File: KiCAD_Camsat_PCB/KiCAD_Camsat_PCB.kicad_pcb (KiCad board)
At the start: 2 copper layers, 92 parts, among them J1 Barrel_Jack, J3 105017-0001, J4 210-1S-1*3Ppin Gold-plated, J5 DZ127R-11-02-25, K1 HYC77-TF09-200, Q1 2N7002T-7-F, Q2 SS8050-G_C164885, Q3 BSS138, Q4 BSS138, Q8 2N7002T-7-F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

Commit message: New PCB design
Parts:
- removed ADDR0: JUMPER-SMT_3_1-NC_TRACE_SILK, Jumper:SolderJumper-2_P1.3mm_Bridged_Pad1.0x1.5mm
- removed C2, C26: 2u2, Capacitor_SMD:C_0603_1608Metric
- removed C21, C7: 100n, Capacitor_SMD:C_0603_1608Metric
- removed C3, C4: 10uF, Capacitor_SMD:C_0805_2012Metric
- removed D2: 1N4148, Diode_SMD:D_SOD-323
- removed D7: SS14, Diode_SMD:D_SMA
- removed J4: 210-1S-1*3Ppin Gold-plated, Connector_PinHeader_2.54mm:PinHeader_1x03_P2.54mm_Vertical
- removed JP1: SMD_JUMPER, Jumper:SolderJumper-2_P1.3mm_Open_Pad1.0x1.5mm
- removed JP9: SMD-JUMPER-CONNECTED_TRACE_SLODERMASK, Jumper:SolderJumper-2_P1.3mm_Bridged_Pad1.0x1.5mm
- removed Q3, Q4: BSS138, Package_TO_SOT_SMD:SOT-23
- removed R1, R5, R6: 10k, Resistor_SMD:R_0805_2012Metric
- removed R26, R27, R7, R8: 10K, Resistor_SMD:R_0805_2012Metric
- removed the R9 at (149.1, 68.8)
- removed the R9 at (189.1, 40.9)
- removed U2: MIC5225-3.3, Package_TO_SOT_SMD:SOT-23-5
- removed U3: SE5218, Package_TO_SOT_SMD:SOT-23-5
- removed U4: TXB0104QPWRQ1, esp32:SOP65P640X120-14N
- added R9: 10K, Resistor_SMD:R_0805_2012Metric, F.Cu at (76.2, 90.0)
- D3, D4, D9: value LESD5D5.0CT1G -> LESD
- J5: value DZ127R-11-02-25 -> DZ127R
- Q1, Q8: value 2N7002T-7-F -> 2N7002T
- Q2, Q9: value SS8050-G_C164885 -> SS8050
- U7: value AMS1117-3.3_C347222 -> AMS1117
- U9: value CP2102N-A02-GQFN28R -> CP2102N
- moved SW2 174.2 mm to (194.5, 72.2)
- moved SW1 168.5 mm to (195.0, 84.0)
- moved C20 158.9 mm to (202.0, 71.5), turned to 90 degrees
- moved D1 155.2 mm to (71.7, 24.0), turned to 0 degrees
- moved Q2 142.8 mm to (192.1, 62.6), turned to -90 degrees
- moved U8 139.8 mm to (164.8, 50.0)
- moved R18 128.5 mm to (191.5, 56.5), turned to 180 degrees
- moved C8 123.8 mm to (95.8, 133.5)
- moved C9 123.8 mm to (95.8, 136.0)
- moved C14 119.1 mm to (155.5, 77.3), turned to 90 degrees
- moved R25 118.7 mm to (106.9, 129.5)
- moved C15 118.7 mm to (146.5, 95.0), turned to 90 degrees
- moved C6 115.3 mm to (95.8, 131.0)
- moved C5 115.3 mm to (95.8, 128.5)
- moved D6 111.0 mm to (148.0, 74.0), turned to 180 degrees
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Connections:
- D1 pad 2: (no net) -> GND
- J1 pad 3: (no net) -> unconnected-(J1-Pad3)
- J3 pad P$1: (no net) -> GND
- J3 pad P$11: (no net) -> GND
- J3 pad P$12: (no net) -> GND
- J3 pad P$13: (no net) -> GND
- J3 pad P$2: (no net) -> GND
- K1 pad 9: (no net) -> unconnected-(K1-X-Pad9)
- K1 pad SHIELD: (no net) -> GND
- U1 pad 9: (no net) -> /INT2
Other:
- board outline added: 76 x 151.5 mm
- board text added: "2026 NAR CAMSAT"

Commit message: traces
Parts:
- moved C37 126.3 mm to (184.7, 70.0)
- moved D1 118.5 mm to (173.0, 85.5)
- moved R29 113.1 mm to (178.0, 44.5), turned to -90 degrees
- moved C8 111.5 mm to (146.5, 34.2), turned to -90 degrees
- moved R10 110.7 mm to (181.5, 59.0)
- moved R16 109.7 mm to (184.1, 56.5)
- moved C6 108.8 mm to (177.7, 59.5)
- moved R3 105.4 mm to (180.6, 70.0)
- moved C9 104.1 mm to (186.0, 84.0), turned to 90 degrees
- moved R20 103.8 mm to (176.5, 38.0), turned to 90 degrees
- moved R9 102.3 mm to (176.5, 70.0)
- moved R15 100.3 mm to (163.5, 33.5)
- moved LED1 99.2 mm to (168.9, 33.5)
- moved R4 95.9 mm to (172.0, 91.0)
- moved C16 93.7 mm to (154.0, 47.5), turned to -90 degrees
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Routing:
- net GND: track 0.00 -> 499.2 mm, vias 0 -> 5
- net +3V3: track 0.00 -> 259.4 mm, vias 0 -> 5
- net /EN: track 0.00 -> 90.1 mm, vias 0 -> 2
- net 3.3V: track 0.00 -> 71.6 mm
- net /IO4: track 0.00 -> 68.9 mm, vias 0 -> 1
- net /RTS: track 0.00 -> 68.8 mm, vias 0 -> 2
- net Net-(Q1-G): track 0.00 -> 68.7 mm, vias 0 -> 2
- net /DTR: track 0.00 -> 67.4 mm, vias 0 -> 2
- net /IO13: track 0.00 -> 65.6 mm, vias 0 -> 2
- net /IO22: track 0.00 -> 50.3 mm, vias 0 -> 5
- net /IO21: track 0.00 -> 49.9 mm, vias 0 -> 3
- net /TXD0: track 0.00 -> 48.7 mm, vias 0 -> 4
- net +5V_VBUS: track 0.00 -> 47.0 mm, vias 0 -> 2
- net /IO0_BTN: track 0.00 -> 46.2 mm, vias 0 -> 2
- net /USB_DP: track 0.00 -> 43.7 mm, vias 0 -> 2
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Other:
- board size 76 x 151.5 mm -> 76 x 78 mm

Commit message: PCB changes
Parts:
- moved R13 66.2 mm to (192.0, 90.0), turned to 90 degrees
- moved J3 2.03 mm to (139.0, 31.0)
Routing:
- net /IO13: track 65.6 -> 51.4 mm
- net /IO0: track 33.5 -> 19.8 mm
- net /EN: track 90.1 -> 103.7 mm, vias 2 -> 3
- net /USB_DP: track 43.7 -> 31.1 mm, vias 2 -> 0
- net /IO4: track 68.9 -> 57.4 mm
- net /RTS: track 68.8 -> 60.9 mm
- net /TXD: track 38.4 -> 45.6 mm, vias 2 -> 6
- net /IO0_BTN: track 46.2 -> 51.8 mm
- net /IO22: track 50.3 -> 55.3 mm, vias 5 -> 4
- net GND: track 499.2 -> 494.5 mm, vias 5 -> 40
- net /TXD0: track 48.7 -> 44.2 mm, vias 4 -> 2
- net /DTR: track 67.4 -> 71.7 mm
- net Net-(Q1-G): track 68.7 -> 64.9 mm, vias 2 -> 1
- net +5V_VBUS: track 47.0 -> 50.6 mm
- net /RXD: track 13.5 -> 17.0 mm, vias 2 -> 0
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- added copper zone on B.Cu, net GND
- added copper zone on F.Cu, net GND
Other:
- board size 76 x 78 mm -> 76 x 80.5 mm
- board text added: "Reset"

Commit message: Prototype
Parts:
- moved R19 5.02 mm to (156.6, 33.8)
- moved D9 3.54 mm to (132.0, 52.5), turned to 0 degrees
- moved D4 3.20 mm to (132.0, 48.8)
- moved C25 0.50 mm to (129.5, 39.5)
- moved J3 0.50 mm to (139.0, 31.5)
- turned D3 to 0 degrees
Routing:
- net /TXD: track 45.6 -> 34.9 mm, vias 6 -> 2
- net /EN: track 103.7 -> 93.6 mm
- net GND: track 494.5 -> 488.7 mm, vias 40 -> 34
- net /IO0_BTN: track 51.8 -> 46.5 mm
- net /USB_DP: track 31.1 -> 26.5 mm
- net /USB_DN: track 31.3 -> 27.6 mm
- net /RXD: track 17.0 -> 19.3 mm
- net +3V3: track 262.6 -> 262.1 mm
- net /TXD0: vias 2 -> 0

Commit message: new changes
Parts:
- removed R19, R20: 0Ω, Resistor_SMD:R_0805_2012Metric
- D3, D4, D9: value LESD -> LESD5D5.0CT1G
- J5: value DZ127R -> DZ127R-11-02-25
- Q1, Q8: value 2N7002T -> 2N7002T-7-F
- Q2, Q9: value SS8050 -> SS8050-G_C164885
- U7: value AMS1117 -> AMS1117-3.3_C347222
- U9: value CP2102N -> CP2102N-A02-GQFN28R
- moved D4 14.7 mm to (140.8, 37.0)
- moved D9 11.9 mm to (138.0, 42.2)
- moved Q1 10.2 mm to (138.6, 37.0), turned to 90 degrees
- moved R21 5.53 mm to (133.5, 45.4)
- moved C17 1.00 mm to (150.0, 48.0)
- moved C16 0.81 mm to (153.2, 47.4)
- moved R11 0.72 mm to (136.6, 48.6)
- moved C25 0.32 mm to (129.6, 39.2), turned to -90 degrees
- moved R22 0.20 mm to (147.2, 48.9)
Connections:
- C37 pad 1: 3.3V -> +3V3
- C5 pad 1: 3.3V -> +3V3
- C6 pad 1: 3.3V -> +3V3
- R2 pad 2: 3.3V -> +3V3
- R25 pad 2: 3.3V -> +3V3
- R3 pad 2: 3.3V -> +3V3
- R39 pad 2: 3.3V -> +3V3
- R4 pad 2: 3.3V -> +3V3
- R9 pad 2: 3.3V -> +3V3
- U1 pad 5: 3.3V -> +3V3
- U1 pad 8: 3.3V -> +3V3
- U10 pad 6: 3.3V -> +3V3
- U10 pad 8: 3.3V -> +3V3
- U8 pad 35: /TXD0 -> /RXD
- U9 pad 26: /TXD -> /RXD0
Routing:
- net GND: track 488.7 -> 0.00 mm, vias 34 -> 0
- net 3.3V: track 69.4 -> 0.00 mm
- net /TXD0: track 44.2 -> 0.00 mm
- net /RXD0: track 16.1 -> 54.0 mm, vias 0 -> 4
- net +3V3: track 262.1 -> 297.0 mm
- net /TXD: track 34.9 -> 0.00 mm, vias 2 -> 0
- net /RXD: track 19.3 -> 43.7 mm, vias 0 -> 2
- net /IO22: track 55.3 -> 41.8 mm, vias 4 -> 3
- net /USB_DP: track 26.5 -> 13.8 mm
- net /USB_DN: track 27.6 -> 37.2 mm, vias 3 -> 2
- net +5V_VBUS: track 50.3 -> 41.8 mm
- net /EN: track 93.6 -> 99.8 mm, vias 3 -> 2
- net /IO5: track 43.2 -> 37.8 mm
- net /IO21: track 48.7 -> 43.7 mm, vias 3 -> 2
- net Net-(Q1-G): track 64.7 -> 69.3 mm
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
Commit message: DRC update
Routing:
- net GND: track 0.00 -> 47.3 mm, vias 0 -> 7
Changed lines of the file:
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@@
 		(tags "SOT-523")
 		(property "Reference" "Q1"
-			(at -2.145 1 0)
+			(at 0.4 -1.6 0)
 			(layer "F.SilkS")
 			(effects
@@
 		(tags "Diode SOD523")
 		(property "Reference" "D4"
-			(at -2.2 0 180)
+			(at 0.4 1.8 180)
 			(layer "F.SilkS")
 			(effects
@@
 	)
 	(segment
+		(start 180.9 44.9)
+		(end 180.9 44.6)
+		(width 0.2)
+		(layer "F.Cu")
+		(net 1)
+	)
+	(segment
+		(start 146.5 33.45)
+		(end 147.75 33.45)
+		(width 0.2)
+		(layer "F.Cu")
+		(net 1)
+	)
+	(segment
+		(start 134.425 48.0375)
+		(end 134.425 45.4)
+		(width 0.2)
+		(layer "F.Cu")
+		(net 1)
+	)
+	(segment
+		(start 136 43.8)
+		(end 137.3 42.5)
+		(width 0.2)
+		(layer "F.Cu")
+		(net 1)
+	)
+	(segment
+		(start 136 43.8)
+		(end 134.425 45.375)
+		(width 0.2)
+		(layer "F.Cu")
+		(net 1)
+	)
+	(segment
+		(start 174.25 46.99)
+		(end 175.44 45.8)
+		(width 0.2)
+		(layer "F.Cu")
+		(net 1)
+	)
+	(segment
+		(start 179.4 46.4)
+		(end 180.9 44.9)
+		(width 0.2)
+		(layer "F.Cu")
+		(net 1)
+	)
+	(segment
+		(start 135.9 49.5125)
+		(end 134.425 48.0375)
+		(width 0.2)
+		(layer "F.Cu")
+		(net 1)
+	)
+	(segment
+		(start 147.75 33.45)
+		(end 149.4 31.8)
+		(width 0.2)
+		(layer "F.Cu")
+		(net 1)
+	)
+	(segment
+		(start 136.6 49.5125)
+		(end 135.9 49.5125)
+		(width 0.2)
+		(layer "F.Cu")
+		(net 1)
+	)
+	(segment
+		(start 134.425 45.375)
+		(end 134.425 45.4)
+		(width 0.2)
+		(layer "F.Cu")
+		(net 1)
+	)
+	(segment
+		(start 175.44 45.8)
+		(end 176 45.8)
+		(width 0.2)
+		(layer "F.Cu")
+		(net 1)
+	)
+	(segment
+		(start 137.3 42.5)
+		(end 137.3 42.2)
+		(width 0.2)
+		(layer "F.Cu")
+		(net 1)
+	)
+	(via
+		(at 131.2 45.6)
+		(size 0.6)
+		(drill 0.3)
+		(layers "F.Cu" "B.Cu")
+		(free yes)
+		(net 1)
+	)
+	(via
+		(at 140.2 39.2)
+		(size 0.6)
+		(drill 0.3)
+		(layers "F.Cu" "B.Cu")
+		(free yes)
+		(net 1)
+	)
+	(via
+		(at 179.4 46.4)
+		(size 0.6)
+		(drill 0.3)
+		(layers "F.Cu" "B.Cu")
+		(net 1)
+	)
+	(via
+		(at 149.4 31.8)
+		(size 0.6)
+		(drill 0.3)
+		(layers "F.Cu" "B.Cu")
+		(free yes)
+		(net 1)
+	)
+	(via
+		(at 136 43.8)
+		(size 0.6)
+		(drill 0.3)
+		(layers "F.Cu" "B.Cu")
+		(free yes)
+		(net 1)
+	)
+	(via
+		(at 176 45.8)
+		(size 0.6)
+		(drill 0.3)
+		(layers "F.Cu" "B.Cu")
+		(net 1)
+	)
+	(via
+		(at 131.2 39.8)
+		(size 0.6)
+		(drill 0.3)
+		(layers "F.Cu" "B.Cu")
+		(free yes)
+		(net 1)
+	)
+	(segment
+		(start 131.2 39.8)
+		(end 131.2 39.5)
+		(width 0.2)
+		(layer "B.Cu")
+		(net 1)
+	)
+	(segment
+		(start 141.5 34.2)
+		(end 142.4 35.1)
+		(width 0.2)
+		(layer "B.Cu")
+		(net 1)
+	)
+	(segment
+		(start 176 45.8)
+		(end 178.8 45.8)
+		(width 0.2)
+		(layer "B.Cu")
+		(net 1)
+	)
+	(segment
+		(start 134.2 45.6)
+		(end 136 43.8)
+		(width 0.2)
+		(layer "B.Cu")
+		(net 1)
+	)
+	(segment
+		(start 142.4 35.1)
+		(end 142.4 37.2)
+		(width 0.2)
+		(layer "B.Cu")
+		(net 1)
+	)
+	(segment
+		(start 140.4 39.2)
+		(end 140.2 39.2)
+		(width 0.2)
+		(layer "B.Cu")
+		(net 1)
+	)
+	(segment
+		(start 131.2 45.6)
+		(end 134.2 45.6)
+		(width 0.2)
+		(layer "B.Cu")
+		(net 1)
+	)
+	(segment
+		(start 131.2 39.8)
+		(end 131.2 45.6)
+		(width 0.2)
+		(layer "B.Cu")
+		(net 1)
+	)
+	(segment
+		(start 131.2 39.5)
+		(end 136.5 34.2)
+		(width 0.2)
+		(layer "B.Cu")
+		(net 1)
+	)
+	(segment
+		(start 178.8 45.8)
+		(end 179.4 46.4)
+		(width 0.2)
+		(layer "B.Cu")
+		(net 1)
+	)
+	(segment
+		(start 142.4 37.2)
+		(end 140.4 39.2)
+		(width 0.2)
+		(layer "B.Cu")
+		(net 1)
+	)
+	(segment

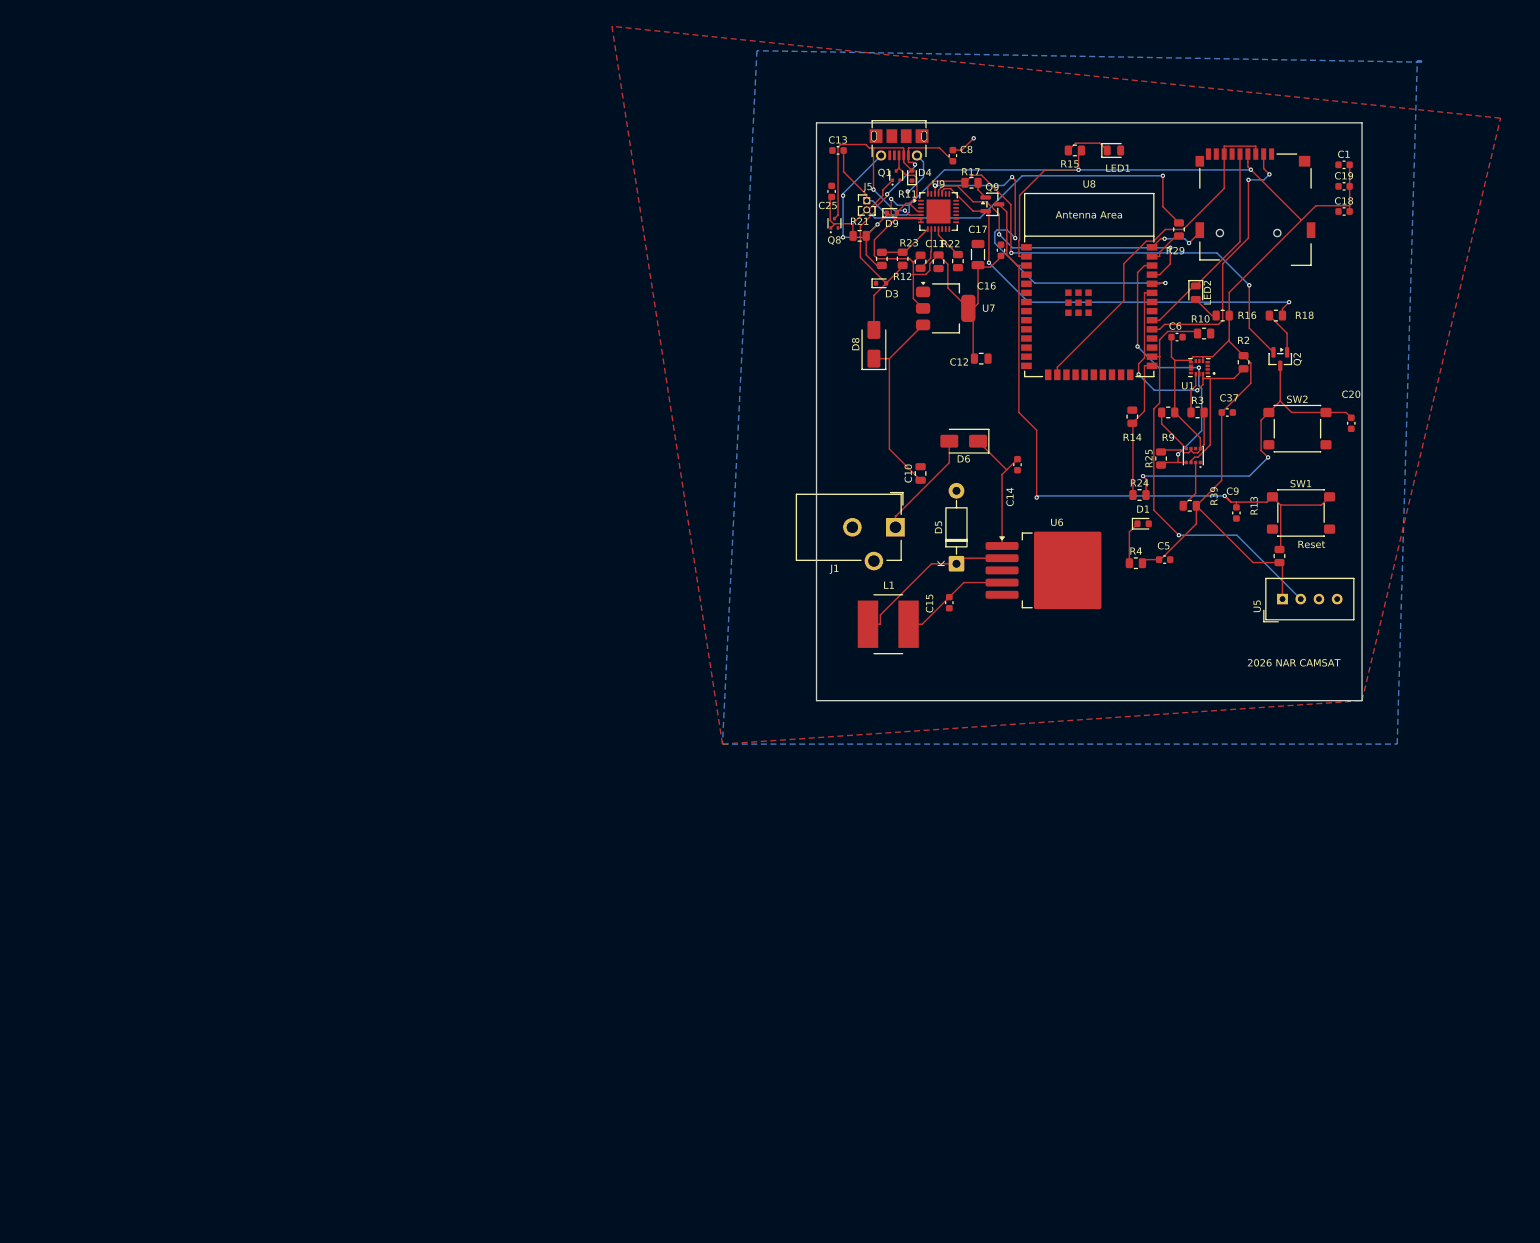
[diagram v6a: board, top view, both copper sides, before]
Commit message: Layout Revision
Removed unnecessary nets.
Added nets for copper pours.
Removed some non-critical components from schematic.
Still needs some extra vias and adjusting silkscreen.
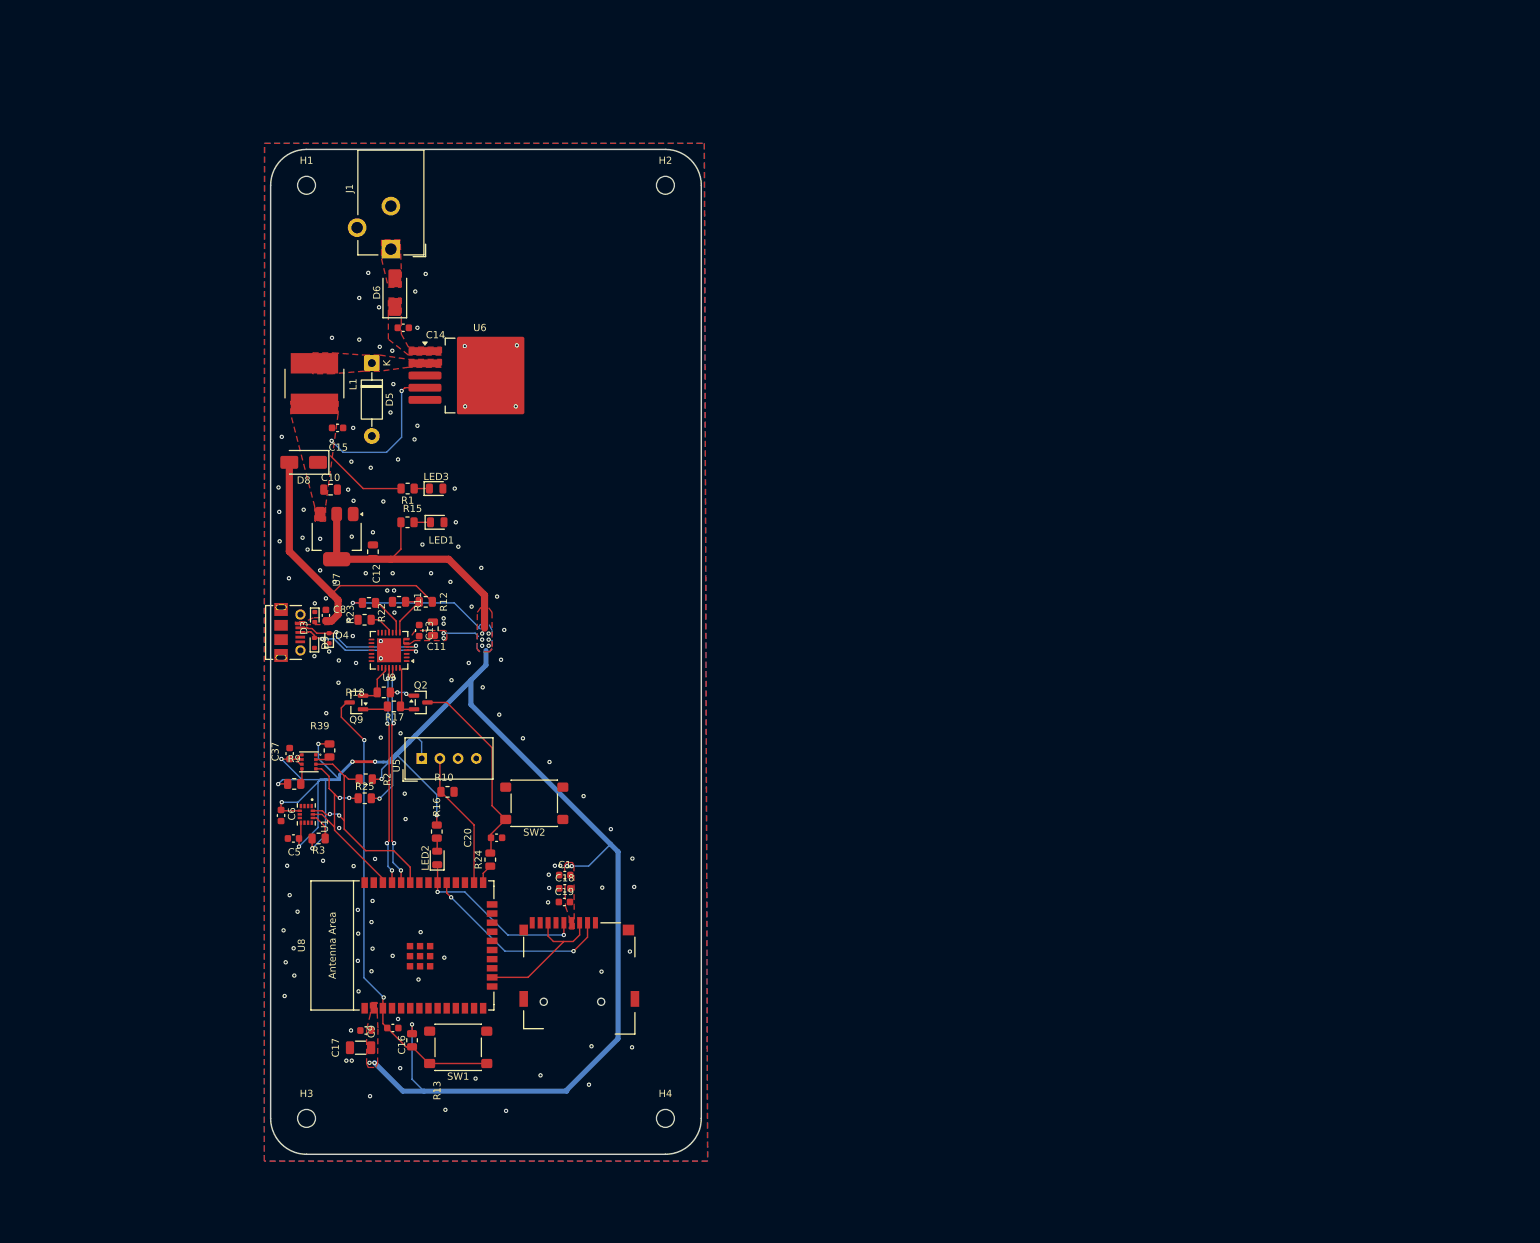
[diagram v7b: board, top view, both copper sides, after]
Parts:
- removed C25: 100nF, Capacitor_SMD:C_0603_1608Metric
- removed D1: RED, LED_SMD:LED_0603_1608Metric
- removed J5: DZ127R-11-02-25, Connector_PinHeader_1.27mm:PinHeader_1x02_P1.27mm_Vertical
- removed Q1, Q8: 2N7002T-7-F, Package_TO_SOT_SMD:SOT-523
- removed R14: 22Ω, Resistor_SMD:R_0805_2012Metric
- removed R21: 10kΩ, Resistor_SMD:R_0805_2012Metric
- removed R29: 1kΩ, Resistor_SMD:R_0805_2012Metric
- removed R4: 1k, Resistor_SMD:R_0805_2012Metric
- added H1: MountingHole, MountingHole:MountingHole_2.5mm, F.Cu at (56.5, 38.4)
- added H2: MountingHole, MountingHole:MountingHole_2.5mm, F.Cu at (106.5, 38.4)
- added H3: MountingHole, MountingHole:MountingHole_2.5mm, F.Cu at (56.5, 168.3)
- added H4: MountingHole, MountingHole:MountingHole_2.5mm, F.Cu at (106.5, 168.3)
- added LED3: 0805G (Green), LED_SMD:LED_0805_2012Metric, F.Cu at (74.5, 80.6)
- added R1: 5.1kΩ, Resistor_SMD:R_0805_2012Metric, F.Cu at (70.5, 80.6)
- moved C19 147.4 mm to (92.4, 138.2)
- moved C1 146.9 mm to (92.4, 134.4)
- moved C18 143.8 mm to (92.4, 136.3)
- moved K1 142.6 mm to (94.5, 148.8)
- moved C6 141.5 mm to (52.9, 126.2), turned to -90 degrees
- moved C16 140.2 mm to (64.7, 156.1), turned to 0 degrees
- moved C17 140.0 mm to (64.0, 158.5), turned to 180 degrees
- moved U1 139.1 mm to (56.4, 126.0), turned to -90 degrees
- moved SW1 139.0 mm to (77.6, 158.4), turned to 180 degrees
- moved C37 139.0 mm to (54.1, 117.5), turned to 90 degrees
- moved R13 138.4 mm to (71.2, 157.5), turned to -90 degrees
- moved C9 137.7 mm to (68.5, 155.8), turned to 180 degrees
- moved R3 136.1 mm to (58.1, 129.3), turned to 180 degrees
- moved R2 135.4 mm to (64.7, 121.1), turned to 0 degrees
- moved R18 134.9 mm to (67.2, 109.0), turned to 0 degrees
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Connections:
- net Net-(D5-K) renamed /5V_out
- net Net-(D6-A) renamed /9V
- net Net-(D6-K) renamed /9VIN
- C15 pad 2: /5V Board -> /5V_Board
- L1 pad 2: /5V Board -> /5V_Board
- U1 pad 10: /OCS -> unconnected-(U1-OCS_AUX-Pad10)
- U6 pad 4: /5V Board -> /5V_Board
- U8 pad 10: /IO25 -> unconnected-(U8-IO25-Pad10)
- U8 pad 11: /IO26 -> unconnected-(U8-IO26-Pad11)
- U8 pad 12: /IO27 -> unconnected-(U8-IO27-Pad12)
- U8 pad 13: /IO14 -> unconnected-(U8-IO14-Pad13)
- U8 pad 14: /IO12 -> unconnected-(U8-IO12-Pad14)
- U8 pad 23: /IO15 -> unconnected-(U8-IO15-Pad23)
- U8 pad 24: /IO2 -> unconnected-(U8-IO2-Pad24)
- U8 pad 27: /IO16 -> unconnected-(U8-IO16-Pad27)
- U8 pad 28: /IO17 -> unconnected-(U8-IO17-Pad28)
- U8 pad 31: /IO19 -> unconnected-(U8-IO19-Pad31)
- U8 pad 37: /IO23 -> unconnected-(U8-IO23-Pad37)
- U8 pad 4: /I36 -> unconnected-(U8-SENSOR_VP-Pad4)
- U8 pad 5: /I39 -> unconnected-(U8-SENSOR_VN-Pad5)
- U8 pad 6: /I34 -> unconnected-(U8-IO34-Pad6)
- U8 pad 7: /I35 -> unconnected-(U8-IO35-Pad7)
- U8 pad 8: /IO32 -> unconnected-(U8-IO32-Pad8)
- U8 pad 9: /IO33 -> unconnected-(U8-IO33-Pad9)
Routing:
- net Net-(Q1-G): track 69.3 -> 0.00 mm, vias 1 -> 0
- net /DTR: track 67.7 -> 7.59 mm, vias 2 -> 0
- net /RTS: track 61.6 -> 6.06 mm, vias 2 -> 0
- net GND: track 47.3 -> 0.00 mm, vias 7 -> 127
- net /IO4: track 56.6 -> 19.3 mm, vias 1 -> 0
- net /EN: track 99.8 -> 64.8 mm
- net /IO13: track 49.0 -> 20.7 mm
- net /5V_out: track 23.2 -> 0.00 mm
- net /RXD0: track 54.0 -> 31.0 mm
- net /9VIN: track 18.6 -> 0.00 mm
- net /IO0_BTN: track 46.4 -> 28.0 mm, vias 2 -> 0
- net /USB_DN: track 37.2 -> 19.2 mm
- net /IO0: track 19.8 -> 2.70 mm
- net /5V Board: track 15.4 -> 0.00 mm
- net /9V: track 15.2 -> 0.00 mm
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- added copper zone on B.Cu, net +3V3
- added copper zone on F.Cu, net +3V3
- added copper zone on F.Cu, net +5V_VBUS
- added copper zone on F.Cu, net /5V_Board
- added copper zone on F.Cu, net /5V_out
- added copper zone on F.Cu, net /9V
- added copper zone on F.Cu, net /9VIN
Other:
- board size 76 x 80.5 mm -> 60 x 140 mm
- board text removed: "2026 NAR CAMSAT"
- board text removed: "Reset"
